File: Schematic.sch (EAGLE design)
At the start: 25 parts, among them IC1 ATTINY85, X1 USBPCB

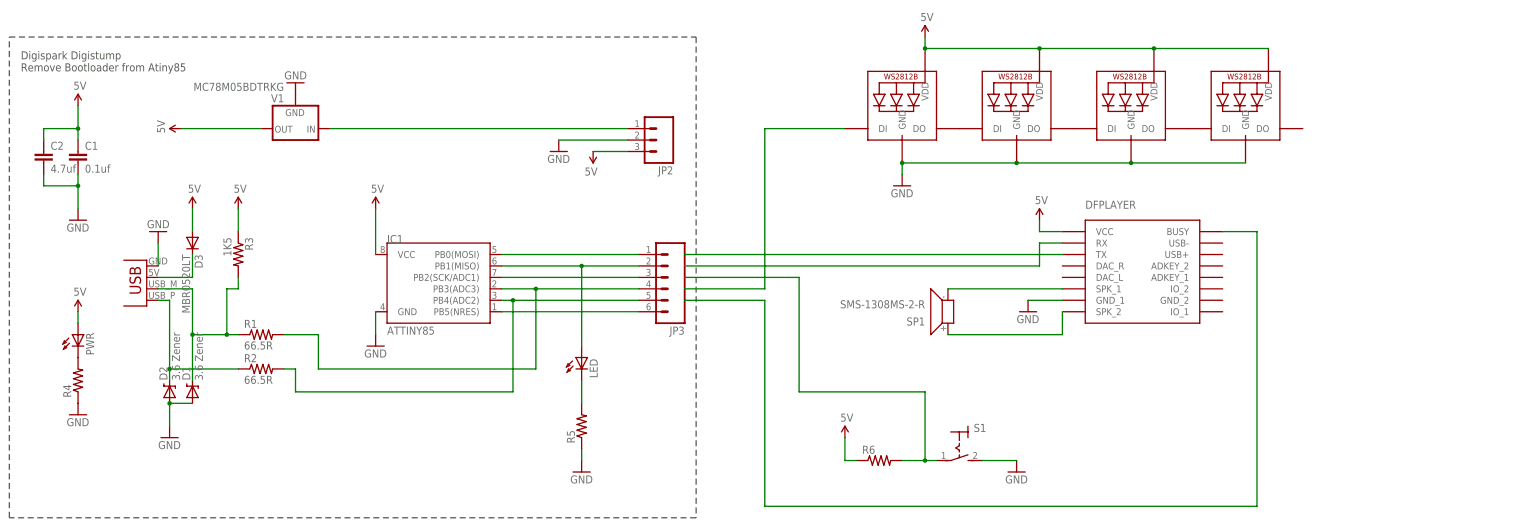
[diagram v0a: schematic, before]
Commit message: Added series resistor in RX line to minimize noise
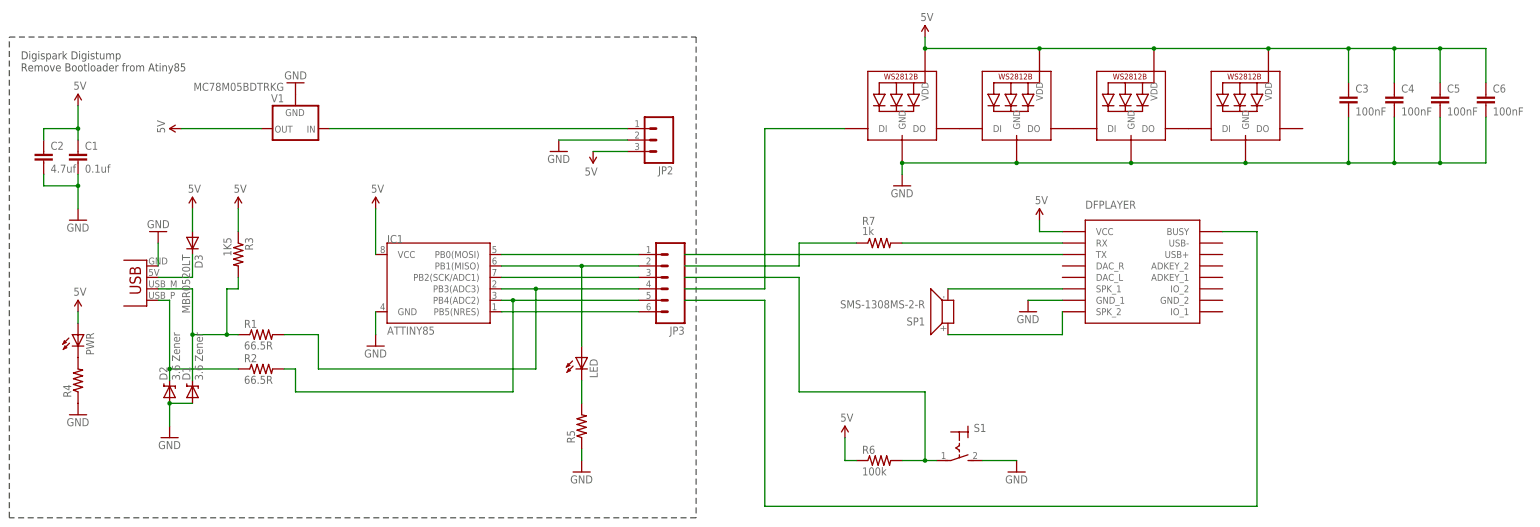
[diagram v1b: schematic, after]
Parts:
- added C3, C4, C5, C6: 100nF, rcl:C-EU102-054X133
- added R7: 1k, SparkFun:RESISTOR0402-RES
- R6: value (none) -> 100k
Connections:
- new net N$23: R7.1
- net 5V: now also C3.1, C4.1, C5.1, C6.1
- net GND: now also C3.2, C4.2, C5.2, C6.2
- net N$19: now also R7.2
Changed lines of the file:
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@@
 <?xml version="1.0" encoding="utf-8"?>
 <!DOCTYPE eagle SYSTEM "eagle.dtd">
-<eagle version="7.6.0">
+<eagle version="7.7.0">
 <drawing>
 <settings>
@@
 <part name="U$9" library="SparkFun" deviceset="5V" device=""/>
 <part name="S1" library="switch" deviceset="MS243" device=""/>
-<part name="R6" library="SparkFun" deviceset="RESISTOR" device="0402-RES"/>
+<part name="R6" library="SparkFun" deviceset="RESISTOR" device="0402-RES" value="100k"/>
 <part name="U$10" library="SparkFun" deviceset="5V" device=""/>
 <part name="GND5" library="SparkFun" deviceset="GND" device=""/>
@@
 <part name="U$11" library="SparkFun" deviceset="5V" device=""/>
 <part name="GND7" library="SparkFun" deviceset="GND" device=""/>
+<part name="R7" library="SparkFun" deviceset="RESISTOR" device="0402-RES" value="1k"/>
+<part name="C3" library="rcl" deviceset="C-EU" device="102-054X133" value="100nF"/>
+<part name="C4" library="rcl" deviceset="C-EU" device="102-054X133" value="100nF"/>
+<part name="C5" library="rcl" deviceset="C-EU" device="102-054X133" value="100nF"/>
+<part name="C6" library="rcl" deviceset="C-EU" device="102-054X133" value="100nF"/>
 </parts>
 <sheets>
@@
 <instance part="U$11" gate="G$1" x="203.2" y="106.68"/>
 <instance part="GND7" gate="1" x="198.12" y="73.66"/>
+<instance part="R7" gate="G$1" x="193.04" y="60.96" smashed="yes">
+<attribute name="NAME" x="189.23" y="64.9986" size="1.778" layer="95"/>
+<attribute name="VALUE" x="189.23" y="62.738" size="1.778" layer="96"/>
+</instance>
+<instance part="C3" gate="G$1" x="297.18" y="93.98"/>
+<instance part="C4" gate="G$1" x="307.34" y="93.98"/>
+<instance part="C5" gate="G$1" x="317.5" y="93.98"/>
+<instance part="C6" gate="G$1" x="327.66" y="93.98"/>
 </instances>
 <busses>
@@
 <wire x1="198.12" y1="76.2" x2="198.12" y2="78.74" width="0.1524" layer="91"/>
 <junction x="198.12" y="78.74"/>
+<pinref part="C6" gate="G$1" pin="2"/>
+<wire x1="274.32" y1="78.74" x2="297.18" y2="78.74" width="0.1524" layer="91"/>
+<wire x1="297.18" y1="78.74" x2="307.34" y2="78.74" width="0.1524" layer="91"/>
+<wire x1="307.34" y1="78.74" x2="317.5" y2="78.74" width="0.1524" layer="91"/>
+<wire x1="317.5" y1="78.74" x2="327.66" y2="78.74" width="0.1524" layer="91"/>
+<wire x1="327.66" y1="78.74" x2="327.66" y2="88.9" width="0.1524" layer="91"/>
+<junction x="274.32" y="78.74"/>
+<pinref part="C5" gate="G$1" pin="2"/>
+<wire x1="317.5" y1="88.9" x2="317.5" y2="78.74" width="0.1524" layer="91"/>
+<junction x="317.5" y="78.74"/>
+<pinref part="C4" gate="G$1" pin="2"/>
+<wire x1="307.34" y1="88.9" x2="307.34" y2="78.74" width="0.1524" layer="91"/>
+<junction x="307.34" y="78.74"/>
+<pinref part="C3" gate="G$1" pin="2"/>
+<wire x1="297.18" y1="88.9" x2="297.18" y2="78.74" width="0.1524" layer="91"/>
+<junction x="297.18" y="78.74"/>
 </segment>
 </net>
@@
 <wire x1="203.2" y1="104.14" x2="203.2" y2="106.68" width="0.1524" layer="91"/>
 <junction x="203.2" y="104.14"/>
+<pinref part="C6" gate="G$1" pin="1"/>
+<wire x1="279.4" y1="104.14" x2="297.18" y2="104.14" width="0.1524" layer="91"/>
+<wire x1="297.18" y1="104.14" x2="307.34" y2="104.14" width="0.1524" layer="91"/>
+<wire x1="307.34" y1="104.14" x2="317.5" y2="104.14" width="0.1524" layer="91"/>
+<wire x1="317.5" y1="104.14" x2="327.66" y2="104.14" width="0.1524" layer="91"/>
+<wire x1="327.66" y1="104.14" x2="327.66" y2="96.52" width="0.1524" layer="91"/>
+<junction x="279.4" y="104.14"/>
+<pinref part="C5" gate="G$1" pin="1"/>
+<wire x1="317.5" y1="96.52" x2="317.5" y2="104.14" width="0.1524" layer="91"/>
+<junction x="317.5" y="104.14"/>
+<pinref part="C4" gate="G$1" pin="1"/>
+<wire x1="307.34" y1="96.52" x2="307.34" y2="104.14" width="0.1524" layer="91"/>
+<junction x="307.34" y="104.14"/>
+<pinref part="C3" gate="G$1" pin="1"/>
+<wire x1="297.18" y1="96.52" x2="297.18" y2="104.14" width="0.1524" layer="91"/>
+<junction x="297.18" y="104.14"/>
 </segment>
 </net>
@@
 <net name="N$19" class="0">
 <segment>
-<wire x1="149.86" y1="55.88" x2="228.6" y2="55.88" width="0.1524" layer="91"/>
-<wire x1="228.6" y1="55.88" x2="228.6" y2="60.96" width="0.1524" layer="91"/>
+<wire x1="198.12" y1="60.96" x2="233.68" y2="60.96" width="0.1524" layer="91"/>
 <pinref part="U$8" gate="G$1" pin="RX"/>
-<wire x1="228.6" y1="60.96" x2="233.68" y2="60.96" width="0.1524" layer="91"/>
+<pinref part="R7" gate="G$1" pin="2"/>
 </segment>
 </net>
@@
 </segment>
 </net>
+<net name="N$23" class="0">
+<segment>
+<wire x1="149.86" y1="55.88" x2="175.26" y2="55.88" width="0.1524" layer="91"/>
+<wire x1="175.26" y1="55.88" x2="175.26" y2="60.96" width="0.1524" layer="91"/>
+<pinref part="R7" gate="G$1" pin="1"/>
+<wire x1="175.26" y1="60.96" x2="187.96" y2="60.96" width="0.1524" layer="91"/>
+</segment>
+</net>
